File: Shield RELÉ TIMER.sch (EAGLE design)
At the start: 54 parts, among them K1 JS-M1-9V-5, K2 JS-M1-9V-5, K3 JS-M1-9V-5, K4 JS-M1-9V-5, K5 JS-M1-9V-5, K6 JS-M1-9V-5, M1 ARDUINO-NANO-3.0, Q1 BC548, Q2 BC548, Q3 BC548, Q4 BC548, Q5 BC548, Q6 BC548

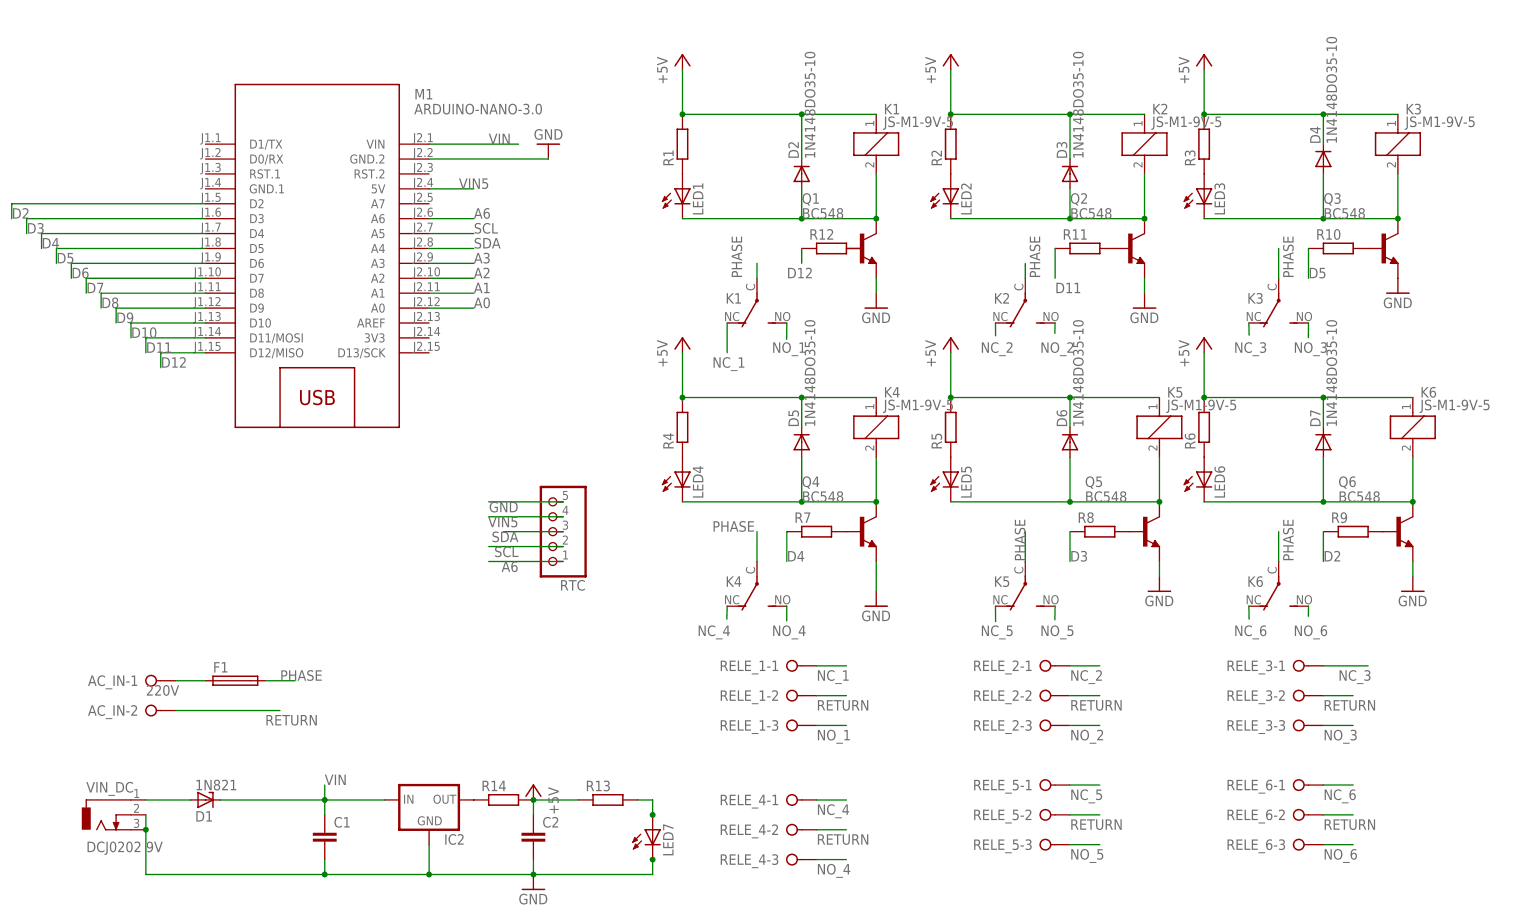
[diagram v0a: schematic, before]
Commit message: Modulo
Separação modulo com reles
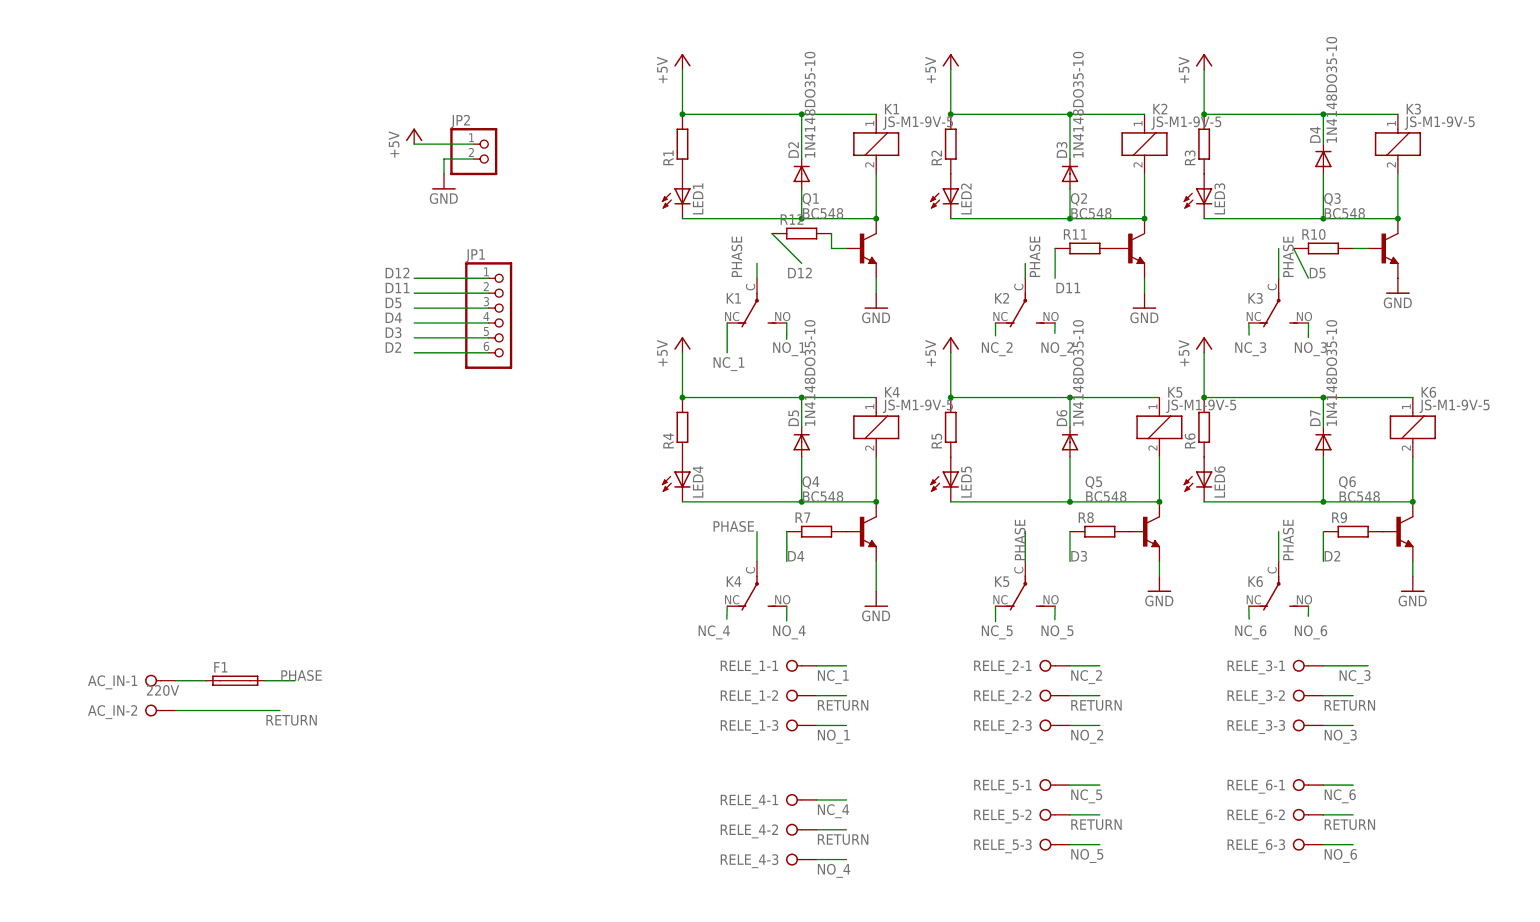
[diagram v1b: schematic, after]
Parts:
- removed C1, C2: (no value), rcl:C-EU025-030X050
- removed D1: 1N821, diode:1N821
- removed IC2: (no value), v-reg:78XXS
- removed LED7: (no value), led:LED5MM
- removed M1: ARDUINO-NANO-3.0, diy-modules:ARDUINO-NANO-3.0
- removed R13: (no value), rcl:R-EU_0204/5
- removed R14: (no value), eagle-ltspice:R0207/10
- removed RTC: (no value), pinhead:PINHD-1X5
- removed VIN_DC: DCJ0202 9V, con-jack:DCJ0202
- added JP1: (no value), pinhead:PINHD-1X6
- added JP2: (no value), pinhead:PINHD-1X2
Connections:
- removed net A0: M1.A0
- removed net A1: M1.A1
- removed net A2: M1.A2
- removed net A3: M1.A3
- removed net A6: M1.A6, RTC.1
- removed net D10: M1.D10
- removed net D6: M1.D6
- removed net D7: M1.D7
- removed net D8: M1.D8
- removed net D9: M1.D9
- removed net N$19: LED7.A, R13.2
- removed net N$20: IC2.OUT, R14.1
- removed net SCL: M1.A5, RTC.2
- removed net SDA: M1.A4, RTC.3
- removed net VIN: C1.1, D1.C, IC2.IN, M1.VIN
- removed net VIN5: M1.5V, RTC.4
- net +5V: now also JP2.1; no longer C2.1, R13.1, R14.2
- net D11: now also JP1.2; no longer M1.D11/MOSI
- net D12: now also JP1.1; no longer M1.D12/MISO
- net D2: now also JP1.6; no longer M1.D2
- net D3: now also JP1.5; no longer M1.D3
- net D4: now also JP1.4; no longer M1.D4
- net D5: now also JP1.3; no longer M1.D5
- net GND: now also JP2.2; no longer C1.2, C2.2, IC2.GND, LED7.C, M1.GND.2, RTC.5, VIN_DC.2, VIN_DC.3
- net N$17: now also Q1.B, R12.2; no longer D1.A, VIN_DC.1
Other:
- moved on the sheet: R10, R12

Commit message: Relay module
Develop three relay module
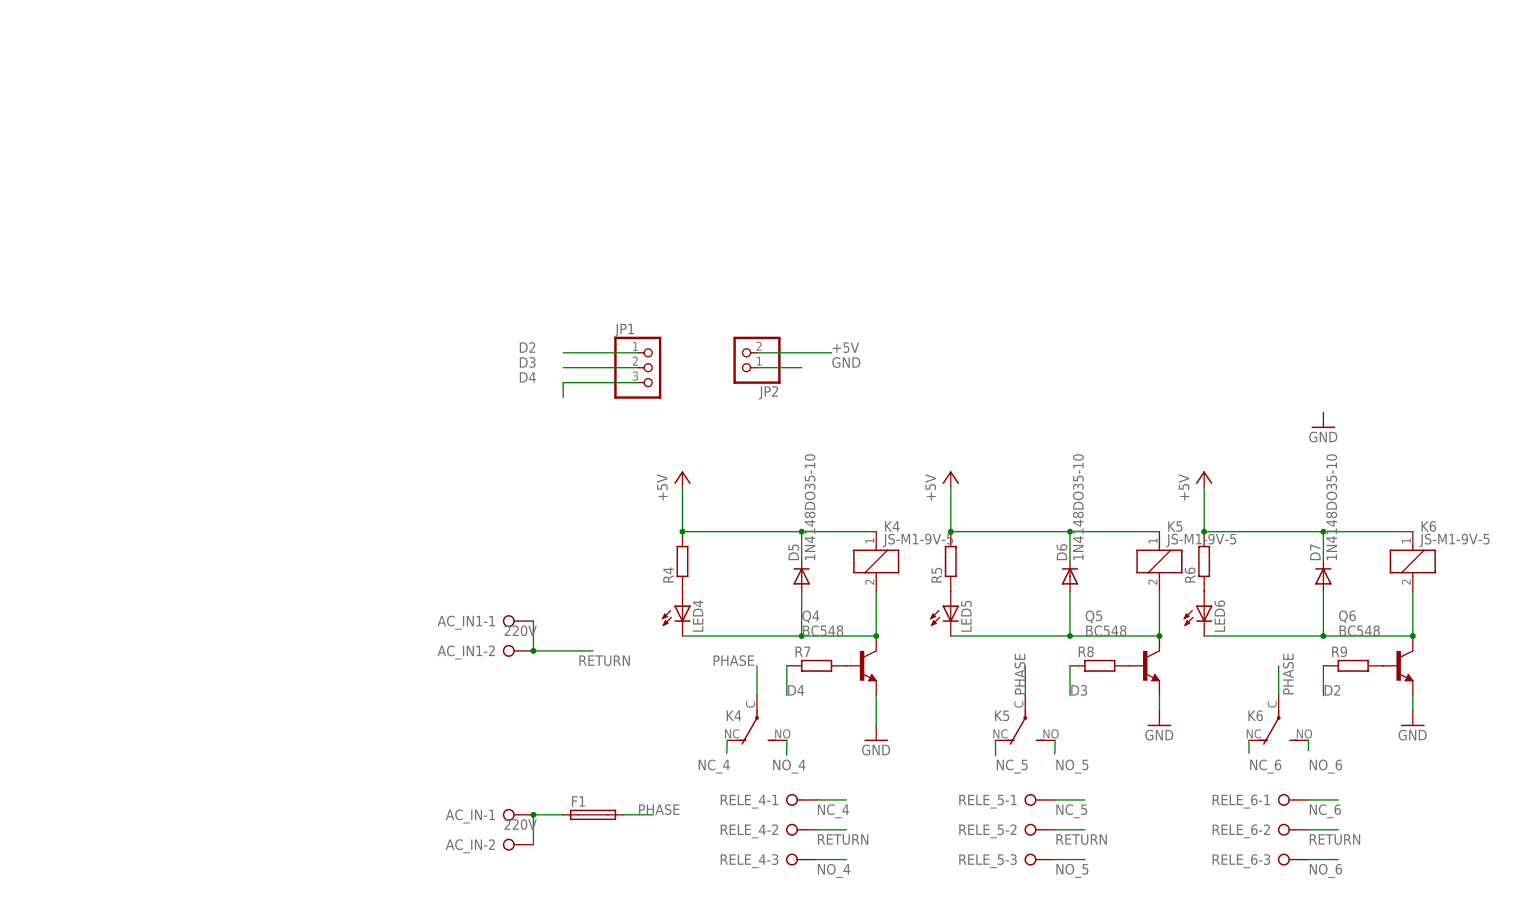
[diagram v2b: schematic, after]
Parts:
- removed D2, D3, D4: 1N4148DO35-10, diode:1N4148DO35-10
- removed K1, K2, K3: JS-M1-9V-5, relay:JS-M1-9V-5
- removed LED1, LED2, LED3: (no value), led:LED5MM
- removed Q1, Q2, Q3: BC548, transistor-npn:BC548
- removed R1, R10, R11, R12, R2, R3: (no value), eagle-ltspice:R0204/7
- removed RELE_1, RELE_2, RELE_3: (no value), con-wago-508:W237-03P
- added AC_IN1: 220V, con-wago-508:W237-02P
- JP1: device pinhead:PINHD-1X6 -> pinhead:PINHD-1X3
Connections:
- removed net D11: JP1.2, R11.1
- removed net D12: JP1.1, R12.1
- removed net D5: JP1.3, R10.1
- removed net N$1: D3.A, K21.2, LED2.C, Q2.C
- removed net N$15: Q3.B, R10.2
- removed net N$17: Q1.B, R12.2
- removed net N$18: Q2.B, R11.2
- removed net N$35: D2.A, K11.2, LED1.C, Q1.C
- removed net N$4: D4.A, K31.2, LED3.C, Q3.C
- removed net N$6: LED1.A, R1.1
- removed net N$8: LED2.A, R2.1
- removed net N$9: LED3.A, R3.1
- removed net NC_1: K12.O, RELE_1-1.KL
- removed net NC_2: K22.O, RELE_2-1.KL
- removed net NC_3: K32.O, RELE_3-1.KL
- removed net NO_1: K12.S, RELE_1-3.KL
- removed net NO_2: K22.S, RELE_2-3.KL
- removed net NO_3: K32.S, RELE_3-3.KL
- net +5V: now also JP2.2; no longer D2.C, D3.C, D4.C, JP2.1, K11.1, K21.1, K31.1, R1.2, R2.2, R3.2
- net D2: now also JP1.1; no longer JP1.6
- net D3: now also JP1.2; no longer JP1.5
- net D4: now also JP1.3; no longer JP1.4
- net GND: now also JP2.1; no longer JP2.2, Q1.E, Q2.E, Q3.E
- net N$16: now also AC_IN-2.KL
- net PHASE: no longer K12.P, K22.P, K32.P
- net RETURN: now also AC_IN1-1.KL, AC_IN1-2.KL; no longer AC_IN-2.KL, RELE_1-2.KL, RELE_2-2.KL, RELE_3-2.KL
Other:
- moved on the sheet: AC_IN-1, AC_IN-2, D5, D6, D7, F1, JP2, K4, K5, K6, LED4, LED5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
